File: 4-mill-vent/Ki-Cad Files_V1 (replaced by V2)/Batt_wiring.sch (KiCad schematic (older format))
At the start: 13 parts, among them J10 Fan, J11 Charger to ext, J12 charger to ext, J13 buzzer, J5 Charger connector, J6 Ext connector, J7 Safety connector cap, J8 Power connector, J9 Ext batt connector

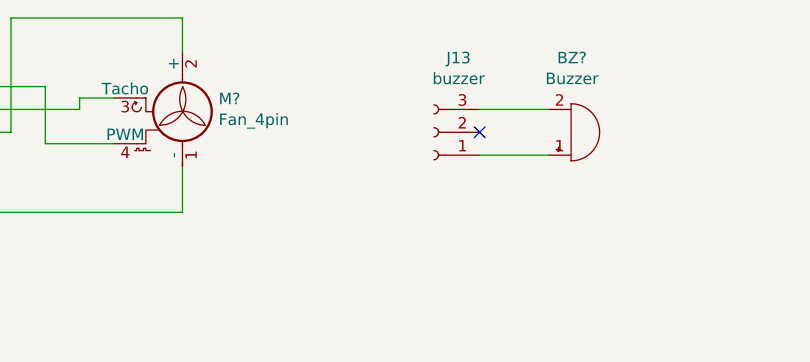
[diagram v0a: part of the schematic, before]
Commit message: Last Update USE V2
Board test complete, all slikscreen error are fixed in v2, Full use of opamp for battery monitoring.
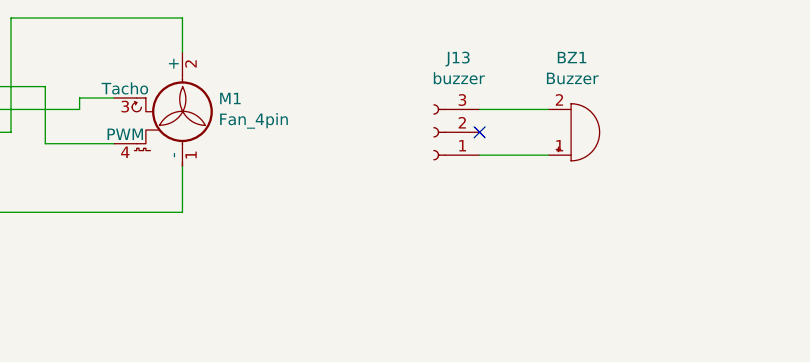
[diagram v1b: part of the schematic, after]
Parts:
- gave numbers to parts that had none: 2
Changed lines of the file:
@@
 $EndSheet
 $Comp
-L Motor:Fan_4pin M?
+L Motor:Fan_4pin M1
 U 1 1 5F20EF18
 P 4950 1450
-F 0 "M?" H 5108 1546 50  0000 L CNN
+F 0 "M1" H 5108 1546 50  0000 L CNN
 F 1 "Fan_4pin" H 5108 1455 50  0000 L CNN
 F 2 "" H 4950 1460 50  0001 C CNN
@@
 	3350 1500 4200 1500
 $Comp
-L Device:Buzzer BZ?
+L Device:Buzzer BZ1
 U 1 1 5F214FCB
 P 6650 1500
-F 0 "BZ?" H 6654 1175 50  0000 C CNN
+F 0 "BZ1" H 6654 1175 50  0000 C CNN
 F 1 "Buzzer" H 6654 1266 50  0000 C CNN
 F 2 "" V 6625 1600 50  0001 C CNN
